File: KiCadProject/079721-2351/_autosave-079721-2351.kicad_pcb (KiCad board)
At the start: 2 copper layers, 227 parts, among them IC1 HC244, IC101 uPC177C, IC201 MP493, IC401 D151811-0360, IC402 IS157, IC501 D151821-0020, IC601 MP5273, IC602 TC4071BP_2, IC603 TC4069UPB_2, J1 Conn_02x13_Odd_Even-MazdaProj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, J2 Conn_02x11_Top_Bottom_Shielde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, J201 Connected, J601 Connected, J711 Empty, Q802 C945, T001 2SB1015B, T211 RN1006, T711 2CS2001, T712 2SD1415, T721 2CS2001, T722 2SD1415, T751 CE1A3Q, T761 CE1A3Q, T801 2CS2001, T803 2CS4065, T811 2CS2001, T812 CE1A3Q, T821 Empty, T822 CE1A3Q (empty), T831 Empty, T832 CE1A3Q (empty), T841 2CS2001, T842 CE1A3Q, T851 Empty, T852 CE1A3Q (empty), T861 Empty, T911 RN1006, T921 RN1006, X601 Crystal

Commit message: Bottom And Top
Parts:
- added J10: Conn_01x01_Female, pinhead-1:pinhead-1-1X01, F.Cu at (196.3, -120.5)
- added J11: Conn_01x01_Female, pinhead-1:pinhead-1-1X01, F.Cu at (200.0, -124.2)
- added J12: Conn_01x01_Female, pinhead-1:pinhead-1-1X01, F.Cu at (203.7, -127.9)
- added J13: Conn_01x01_Female, pinhead-1:pinhead-1-1X01, F.Cu at (192.6, -113.1)
- added J14: Conn_01x01_Female, pinhead-1:pinhead-1-1X01, F.Cu at (196.3, -116.8)
- added J15: Conn_01x01_Female, pinhead-1:pinhead-1-1X01, F.Cu at (200.0, -120.5)
- added J16: Conn_01x01_Female, pinhead-1:pinhead-1-1X01, F.Cu at (203.7, -124.2)
- added J17: Conn_01x01_Female, pinhead-1:pinhead-1-1X01, F.Cu at (207.4, -127.9)
- added J18: Conn_01x01_Female, pinhead-1:pinhead-1-1X01, F.Cu at (196.3, -113.1)
- added J19: Conn_01x01_Female, pinhead-1:pinhead-1-1X01, F.Cu at (200.0, -116.8)
- added J20: Conn_01x01_Female, pinhead-1:pinhead-1-1X01, F.Cu at (203.7, -120.5)
- added J21: Conn_01x01_Female, pinhead-1:pinhead-1-1X01, F.Cu at (207.4, -124.2)
- added J22: Conn_01x01_Female, pinhead-1:pinhead-1-1X01, F.Cu at (211.1, -127.9)
- added J23: Conn_01x01_Female, pinhead-1:pinhead-1-1X01, F.Cu at (200.0, -113.1)
- added J24: Conn_01x01_Female, pinhead-1:pinhead-1-1X01, F.Cu at (203.7, -116.8)
- added J25: Conn_01x01_Female, pinhead-1:pinhead-1-1X01, F.Cu at (207.4, -120.5)
- added J26: Conn_01x01_Female, pinhead-1:pinhead-1-1X01, F.Cu at (211.1, -124.2)
- added J27: Conn_01x01_Female, pinhead-1:pinhead-1-1X01, F.Cu at (214.7, -127.9)
- added J28: Conn_01x01_Female, pinhead-1:pinhead-1-1X01, F.Cu at (203.7, -113.1)
- added J29: Conn_01x01_Female, pinhead-1:pinhead-1-1X01, F.Cu at (207.4, -116.8)
- added J3: Conn_01x01_Female, pinhead-1:pinhead-1-1X01, F.Cu at (184.5, -132.5)
- added J30: Conn_01x01_Female, pinhead-1:pinhead-1-1X01, F.Cu at (211.1, -120.5)
- added J31: Conn_01x01_Female, pinhead-1:pinhead-1-1X01, F.Cu at (214.7, -124.2)
- added J32: Conn_01x01_Female, pinhead-1:pinhead-1-1X01, F.Cu at (218.4, -127.9)
- added J33: Conn_01x01_Female, pinhead-1:pinhead-1-1X01, F.Cu at (207.4, -113.1)
- added J34: Conn_01x01_Female, pinhead-1:pinhead-1-1X01, F.Cu at (211.1, -116.8)
- added J35: Conn_01x01_Female, pinhead-1:pinhead-1-1X01, F.Cu at (214.7, -120.5)
- added J36: Conn_01x01_Female, pinhead-1:pinhead-1-1X01, F.Cu at (218.4, -124.2)
- added J37: Conn_01x01_Female, pinhead-1:pinhead-1-1X01, F.Cu at (222.1, -127.9)
- added J38: Conn_01x01_Female, pinhead-1:pinhead-1-1X01, F.Cu at (211.1, -113.1)
- added J4: Conn_01x01_Female, pinhead-1:pinhead-1-1X01, F.Cu at (188.8, -132.7)
- added J5: Conn_01x01_Female, pinhead-1:pinhead-1-1X01, F.Cu at (196.3, -127.9)
- added J6: Conn_01x01_Female, pinhead-1:pinhead-1-1X01, F.Cu at (192.6, -120.5)
- added J7: Conn_01x01_Female, pinhead-1:pinhead-1-1X01, F.Cu at (196.3, -124.2)
- added J8: Conn_01x01_Female, pinhead-1:pinhead-1-1X01, F.Cu at (200.0, -127.9)
- added J9: Conn_01x01_Female, pinhead-1:pinhead-1-1X01, F.Cu at (192.6, -116.8)
- moved IC201 42.1 mm to (406.7, 26.8)
- renumbered T001 to T1
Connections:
- C2 pad 1: Net-(C2-Pad1) -> Net-(C1-Pad1)
- C4 pad 1: Net-(C4-Pad1) -> Net-(C3-Pad1)
- C422 pad 2: Net-(C422-Pad2) -> Net-(C411-Pad2)
- C451 pad 2: Net-(C451-Pad2) -> Net-(C431-Pad1)
- C452 pad 2: Net-(C452-Pad2) -> Net-(C442-Pad1)
- C471 pad 2: Net-(C471-Pad2) -> Net-(C441-Pad1)
- C472 pad 1: Net-(C472-Pad1) -> Net-(C461-Pad1)
- C502 pad 1: Net-(C502-Pad1) -> Net-(C501-Pad1)
- C502 pad 2: Net-(C502-Pad2) -> Net-(C501-Pad2)
- C503 pad 1: Net-(C503-Pad1) -> Net-(C105-Pad1)
- C504 pad 1: Net-(C504-Pad1) -> Net-(C105-Pad1)
- C511 pad 2: Net-(C511-Pad2) -> Net-(C501-Pad1)
- C52 pad 1: Net-(C52-Pad1) -> GND
- C53 pad 2: Net-(C53-Pad2) -> GND
- C54 pad 2: Net-(C54-Pad2) -> GND
- C55 pad 2: Net-(C55-Pad2) -> GND
- C6 pad 1: Net-(C6-Pad1) -> Net-(C5-Pad1)
- C6 pad 2: Net-(C6-Pad2) -> Net-(C5-Pad2)
- C604 pad 2: Net-(C604-Pad2) -> Net-(C501-Pad1)
- C606 pad 1: Net-(C606-Pad1) -> Net-(C501-Pad1)
- C607 pad 1: Net-(C607-Pad1) -> Net-(C605-Pad1)
- C607 pad 2: Net-(C607-Pad2) -> Net-(C605-Pad2)
- C8 pad 1: Net-(C8-Pad1) -> Net-(C603-Pad2)
- D1 pad 2: Net-(D1-Pad2) -> Net-(C55-Pad1)
- D3 pad 2: Net-(D3-Pad2) -> Net-(C1-Pad1)
- D4 pad 1: Net-(D4-Pad1) -> Net-(C1-Pad1)
- IC1 pad 1: Net-(IC1-Pad1) -> Net-(C1-Pad1)
- IC1 pad 11: Net-(IC1-Pad11) -> Net-(C9-Pad2)
- IC1 pad 4: Net-(IC1-Pad4) -> Net-(C5-Pad1)
- IC101 pad 10: Net-(IC101-Pad10) -> Net-(C101-Pad2)
- IC101 pad 3: Net-(IC101-Pad3) -> Net-(C105-Pad2)
- IC101 pad 5: Net-(IC101-Pad5) -> Net-(C504-Pad2)
- IC101 pad 8: Net-(IC101-Pad8) -> Net-(C111-Pad1)
- IC401 pad 10: Net-(IC401-Pad10) -> Net-(C442-Pad2)
- IC401 pad 11: Net-(IC401-Pad11) -> Net-(C432-Pad1)
- IC401 pad 12: Net-(IC401-Pad12) -> Net-(C422-Pad1)
- IC401 pad 15: Net-(IC401-Pad15) -> Net-(C405-Pad1)
- IC401 pad 16: Net-(IC401-Pad16) -> Net-(C405-Pad1)
- IC401 pad 18: Net-(IC401-Pad18) -> Net-(C405-Pad2)
- IC401 pad 19: Net-(IC401-Pad19) -> Net-(C491-Pad2)
- IC401 pad 7: Net-(IC401-Pad7) -> Net-(C472-Pad2)
- IC401 pad 8: Net-(IC401-Pad8) -> Net-(C461-Pad2)
- IC401 pad 9: Net-(IC401-Pad9) -> Net-(C452-Pad1)
- IC402 pad 6: Net-(IC402-Pad6) -> Net-(C405-Pad1)
- IC501 pad 13: Net-(IC501-Pad13) -> Net-(C502-Pad7)
- IC501 pad 14: Net-(IC501-Pad14) -> Net-(C501-Pad7)
- IC501 pad 15: Net-(IC501-Pad15) -> Net-(C501-Pad6)
- IC501 pad 16: Net-(IC501-Pad16) -> Net-(C502-Pad5)
- IC501 pad 17: Net-(IC501-Pad17) -> Net-(C501-Pad5)
- IC501 pad 18: Net-(IC501-Pad18) -> Net-(C501-Pad4)
- IC501 pad 19: Net-(IC501-Pad19) -> Net-(C501-Pad3)
- IC501 pad 20: Net-(IC501-Pad20) -> Net-(C501-Pad2)
- IC601 pad 11: Net-(IC601-Pad11) -> Net-(IC101-Pad1)
- IC601 pad 12: Net-(IC601-Pad12) -> Net-(IC501-Pad6)
- IC601 pad 14: Net-(IC601-Pad14) -> Net-(IC501-Pad4)
- IC601 pad 15: Net-(IC601-Pad15) -> Net-(IC501-Pad5)
- IC601 pad 16: Net-(IC601-Pad16) -> Net-(IC501-Pad10)
- IC601 pad 28: Net-(IC601-Pad28) -> Net-(IC1-Pad12)
- IC601 pad 32: Net-(IC601-Pad32) -> Net-(IC401-Pad23)
- IC601 pad 33: Net-(IC601-Pad33) -> Net-(IC401-Pad22)
- IC601 pad 34: Net-(IC601-Pad34) -> Net-(IC401-Pad21)
- IC601 pad 39: Net-(IC601-Pad39) -> Net-(C9-Pad1)
- IC602 pad 14: Net-(IC602-Pad14) -> Net-(C605-Pad1)
- IC602 pad 3: Net-(IC602-Pad3) -> Net-(IC201-Pad7)
- IC602 pad 4: Net-(IC602-Pad4) -> Net-(IC201-Pad4)
- IC602 pad 5: Net-(IC602-Pad5) -> Net-(IC602-Pad2)
- IC602 pad 9: Net-(IC602-Pad9) -> Net-(IC602-Pad2)
- IC603 pad 1: Net-(IC603-Pad1) -> Net-(IC101-Pad13)
- IC603 pad 14: Net-(IC603-Pad14) -> Net-(C605-Pad1)
- IC603 pad 5: Net-(IC603-Pad5) -> Net-(IC401-Pad17)
- IC603 pad 6: Net-(IC603-Pad6) -> Net-(IC602-Pad12)
- IC603 pad 9: Net-(IC603-Pad9) -> Net-(IC101-Pad14)
- J1 pad 2B: Net-(J1-Pad2B) -> Net-(J1-Pad2A)
- J1 pad 2K: Net-(J1-Pad2K) -> Net-(F401-Pad1)
- J1 pad 2M: Net-(J1-Pad2M) -> Net-(C441-Pad2)
- J1 pad 2O: Net-(J1-Pad2O) -> Net-(C451-Pad1)
- J1 pad 2P: Net-(J1-Pad2P) -> Net-(C421-Pad2)
- J1 pad 2Q: Net-(J1-Pad2Q) -> Net-(C431-Pad2)
- J2 pad B: Net-(J2-PadB) -> Net-(C56-Pad1)
- J2 pad D: Net-(J2-PadD) -> Net-(C911-Pad1)
- J2 pad F: Net-(J2-PadF) -> Net-(C921-Pad1)
- J2 pad M: Net-(J2-PadM) -> Net-(J2-PadL)
- J2 pad T: Net-(J2-PadT) -> Net-(J1-Pad2I)
- J201 pad 1: Net-(J201-Pad1) -> Net-(IC201-Pad2)
- J601 pad 1: Net-(J601-Pad1) -> Net-(IC1-Pad7)
- J601 pad 2: Net-(J601-Pad2) -> Net-(IC601-Pad29)
- J711 pad 1: Net-(J711-Pad1) -> Net-(C721-Pad2)
- J711 pad 2: Net-(J711-Pad2) -> Net-(C711-Pad2)
- R1 pad 1: Net-(R1-Pad1) -> Net-(IC1-Pad2)
- R101 pad 1: Net-(R101-Pad1) -> Net-(J1-Pad2E)
- R102 pad 1: Net-(R102-Pad1) -> Net-(C101-Pad2)
- R102 pad 2: Net-(R102-Pad2) -> Net-(J1-Pad2E)
- R104 pad 1: Net-(R104-Pad1) -> Net-(C101-Pad1)
- R104 pad 2: Net-(R104-Pad2) -> Net-(IC101-Pad11)
- R105 pad 1: Net-(R105-Pad1) -> Net-(IC101-Pad13)
- R105 pad 2: Net-(R105-Pad2) -> Net-(IC101-Pad11)
- R106 pad 1: Net-(R106-Pad1) -> Net-(C405-Pad1)
- R111 pad 1: Net-(R111-Pad1) -> Net-(J1-Pad2G)
- R112 pad 1: Net-(R112-Pad1) -> Net-(C111-Pad1)
- R112 pad 2: Net-(R112-Pad2) -> Net-(J1-Pad2G)
- R114 pad 2: Net-(R114-Pad2) -> Net-(C101-Pad1)
- R115 pad 2: Net-(R115-Pad2) -> Net-(IC101-Pad14)
- R116 pad 1: Net-(R116-Pad1) -> Net-(C405-Pad1)
- R2 pad 2: Net-(R2-Pad2) -> Net-(C9-Pad1)
- R204 pad 1: Net-(R204-Pad1) -> Net-(IC201-Pad24)
- R21 pad 1: Net-(R21-Pad1) -> Net-(C1-Pad1)
- R401 pad 1: Net-(R401-Pad1) -> Net-(J1-Pad2N)
- R402 pad 1: Net-(R402-Pad1) -> Net-(C401-Pad2)
- R414 pad 1: Net-(R414-Pad1) -> Net-(IC401-Pad13)
- R422 pad 1: Net-(R422-Pad1) -> Net-(C422-Pad1)
- R422 pad 2: Net-(R422-Pad2) -> Net-(C421-Pad2)
- R431 pad 1: Net-(R431-Pad1) -> Net-(C431-Pad2)
- R432 pad 1: Net-(R432-Pad1) -> Net-(C432-Pad1)
- R441 pad 2: Net-(R441-Pad2) -> Net-(C441-Pad2)
- R442 pad 1: Net-(R442-Pad1) -> Net-(C442-Pad2)
- R442 pad 2: Net-(R442-Pad2) -> Net-(C441-Pad2)
- R451 pad 1: Net-(R451-Pad1) -> Net-(C451-Pad1)
- R452 pad 1: Net-(R452-Pad1) -> Net-(C452-Pad1)
- R452 pad 2: Net-(R452-Pad2) -> Net-(C451-Pad1)
- R461 pad 1: Net-(R461-Pad1) -> Net-(C405-Pad1)
- R461 pad 2: Net-(R461-Pad2) -> Net-(IC402-Pad7)
- R471 pad 1: Net-(R471-Pad1) -> Net-(J1-Pad2L)
- R472 pad 1: Net-(R472-Pad1) -> Net-(C472-Pad2)
- R481 pad 1: Net-(R481-Pad1) -> Net-(R111-Pad2)
- R481 pad 2: Net-(R481-Pad2) -> Net-(J1-Pad2J)
- R482 pad 2: Net-(R482-Pad2) -> Net-(J1-Pad2J)
- R483 pad 1: Net-(R483-Pad1) -> Net-(R412-Pad2)
- R483 pad 2: Net-(R483-Pad2) -> Net-(C481-Pad2)
- R491 pad 2: Net-(R491-Pad2) -> Net-(J1-Pad2H)
- R492 pad 1: Net-(R492-Pad1) -> Net-(C491-Pad2)
- R492 pad 2: Net-(R492-Pad2) -> Net-(J1-Pad2H)
- R493 pad 1: Net-(R493-Pad1) -> Net-(C491-Pad2)
- R501 pad 2: Net-(R501-Pad2) -> Net-(J2-PadP)
- R502 pad 2: Net-(R502-Pad2) -> Net-(J2-PadU)
- R506 pad 1: Net-(R506-Pad1) -> Net-(J2-PadS)
- R507 pad 2: Net-(R507-Pad2) -> Net-(J2-PadO)
- R509 pad 2: Net-(R509-Pad2) -> Net-(J1-Pad2I)
- R510 pad 1: Net-(R510-Pad1) -> Net-(J1-Pad2I)
- R511 pad 2: Net-(R511-Pad2) -> Net-(J2-PadU)
- R512 pad 2: Net-(R512-Pad2) -> Net-(J2-PadO)
- R513 pad 1: Net-(R513-Pad1) -> Net-(C501-Pad6)
- R514 pad 1: Net-(R514-Pad1) -> Net-(C502-Pad5)
- R514 pad 2: Net-(R514-Pad2) -> Net-(J2-PadN)
- R515 pad 2: Net-(R515-Pad2) -> Net-(R505-Pad2)
- R516 pad 1: Net-(R516-Pad1) -> Net-(C501-Pad4)
- R516 pad 2: Net-(R516-Pad2) -> Net-(R504-Pad2)
- R517 pad 2: Net-(R517-Pad2) -> Net-(R503-Pad2)
- R518 pad 2: Net-(R518-Pad2) -> Net-(J2-PadP)
- R519 pad 2: Net-(R519-Pad2) -> Net-(J1-Pad2I)
- R520 pad 2: Net-(R520-Pad2) -> Net-(R508-Pad2)
- R531 pad 2: Net-(R531-Pad2) -> Net-(J2-PadV)
- R532 pad 1: Net-(R532-Pad1) -> Net-(J2-PadR)
- R541 pad 2: Net-(R541-Pad2) -> Net-(J2-PadV)
- R542 pad 2: Net-(R542-Pad2) -> Net-(J2-PadR)
- R561 pad 1: Net-(R561-Pad1) -> Net-(IC101-Pad6)
- R562 pad 1: Net-(R562-Pad1) -> Net-(C105-Pad1)
- R601 pad 3: Net-(R601-Pad3) -> Net-(IC601-Pad8)
- R601 pad 4: Net-(R601-Pad4) -> Net-(IC601-Pad7)
- R601 pad 6: Net-(R601-Pad6) -> Net-(IC601-Pad37)
- R601 pad 7: Net-(R601-Pad7) -> Net-(IC601-Pad38)
- R601 pad 8: Net-(R601-Pad8) -> Net-(IC601-Pad40)
- R601 pad 9: Net-(R601-Pad9) -> Net-(IC601-Pad42)
- R602 pad 1: Net-(R602-Pad1) -> Net-(IC601-Pad19)
- R602 pad 2: Net-(R602-Pad2) -> Net-(IC101-Pad1)
- R602 pad 3: Net-(R602-Pad3) -> Net-(IC601-Pad10)
- R602 pad 4: Net-(R602-Pad4) -> Net-(IC101-Pad13)
- R602 pad 5: Net-(R602-Pad5) -> Net-(C405-Pad1)
- R602 pad 6: Net-(R602-Pad6) -> Net-(IC101-Pad14)
- R602 pad 7: Net-(R602-Pad7) -> Net-(IC601-Pad6)
- R602 pad 8: Net-(R602-Pad8) -> Net-(IC601-Pad5)
- R602 pad 9: Net-(R602-Pad9) -> Net-(IC603-Pad11)
- R712 pad 2: Net-(R712-Pad2) -> Net-(R711-Pad2)
- R722 pad 1: Net-(R722-Pad1) -> Net-(R721-Pad2)
- R763 pad 1: Net-(R763-Pad1) -> Net-(R753-Pad1)
- R802 pad 2: Net-(R802-Pad2) -> Net-(D801-Pad1)
- R803 pad 1: Net-(R803-Pad1) -> Net-(R801-Pad2)
- R803 pad 2: Net-(R803-Pad2) -> Net-(Q802-Pad1)
- R804 pad 2: Net-(R804-Pad2) -> Net-(Q802-Pad1)
- R807 pad 1: Net-(R807-Pad1) -> Net-(D802-Pad2)
- R812 pad 1: Net-(R812-Pad1) -> Net-(D812-Pad2)
- R812 pad 2: Net-(R812-Pad2) -> Net-(J1-Pad2X)
- R813 pad 2: Net-(R813-Pad2) -> Net-(D811-Pad2)
- R822 pad 1: Net-(R822-Pad1) -> Net-(D821-Pad2)
- R822 pad 2: Net-(R822-Pad2) -> Net-(J1-Pad2S)
- R832 pad 1: Net-(R832-Pad1) -> Net-(D831-Pad2)
- R832 pad 2: Net-(R832-Pad2) -> Net-(J1-Pad2T)
- R842 pad 2: Net-(R842-Pad2) -> Net-(J2-PadJ)
- R861 pad 2: Net-(R861-Pad2) -> Net-(J1-Pad2Y)
- R912 pad 1: Net-(R912-Pad1) -> Net-(C1-Pad1)
- R913 pad 2: Net-(R913-Pad2) -> Net-(C911-Pad1)
- R923 pad 2: Net-(R923-Pad2) -> Net-(C921-Pad1)
- R924 pad 2: Net-(R924-Pad2) -> Net-(J2-PadE)
- T1 pad 2: Net-(T001-Pad2) -> Net-(C5-Pad1)
- T1 pad 3: Net-(T001-Pad3) -> Net-(IC1-Pad2)
- T711 pad 1: Net-(T711-Pad1) -> Net-(IC201-Pad24)
- T711 pad 3: Net-(T711-Pad3) -> Net-(IC201-Pad19)
- T712 pad 1: Net-(T712-Pad1) -> Net-(R711-Pad2)
- T721 pad 1: Net-(T721-Pad1) -> Net-(IC201-Pad24)
- T721 pad 3: Net-(T721-Pad3) -> Net-(IC201-Pad18)
- T722 pad 1: Net-(T722-Pad1) -> Net-(R721-Pad2)
- T751 pad 1: Net-(T751-Pad1) -> Net-(J1-Pad2C)
- T761 pad 1: Net-(T761-Pad1) -> Net-(J1-Pad2C)
- T801 pad 1: Net-(T801-Pad1) -> Net-(IC201-Pad24)
- T801 pad 3: Net-(T801-Pad3) -> Net-(IC201-Pad17)
- T803 pad 2: Net-(T803-Pad2) -> Net-(R807-Pad2)
- T811 pad 1: Net-(T811-Pad1) -> Net-(R761-Pad2)
- T811 pad 3: Net-(T811-Pad3) -> Net-(R814-Pad1)
- T812 pad 3: Net-(T812-Pad3) -> Net-(R811-Pad2)
- T821 pad 1: Net-(T821-Pad1) -> Net-(R761-Pad2)
- T821 pad 3: Net-(T821-Pad3) -> Net-(R823-Pad1)
- T822 pad 3: Net-(T822-Pad3) -> Net-(R821-Pad2)
- T831 pad 1: Net-(T831-Pad1) -> Net-(R761-Pad2)
- T831 pad 3: Net-(T831-Pad3) -> Net-(R833-Pad1)
- T841 pad 1: Net-(T841-Pad1) -> Net-(R761-Pad2)
- T841 pad 3: Net-(T841-Pad3) -> Net-(R843-Pad1)
- T851 pad 1: Net-(T851-Pad1) -> Net-(IC201-Pad24)
- T911 pad 1: Net-(T911-Pad1) -> Net-(C7-Pad2)
- c51 pad 2: Net-(c51-Pad2) -> GND
- c861 pad 1: Net-(c861-Pad1) -> Net-(J1-Pad2Y)

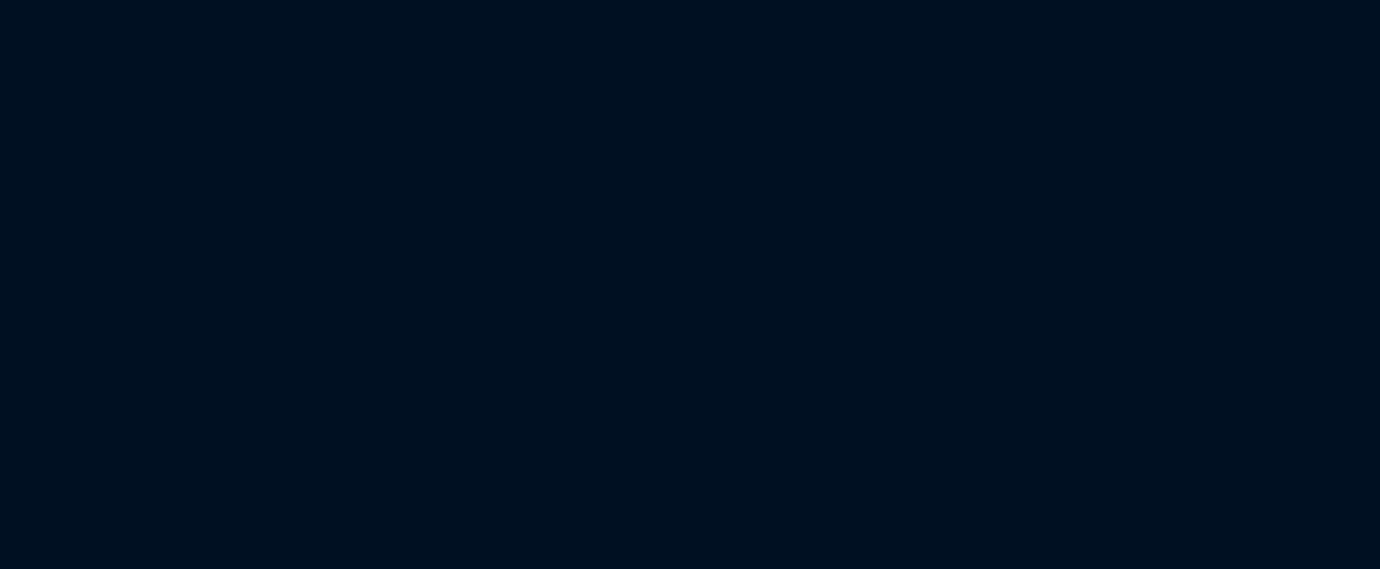
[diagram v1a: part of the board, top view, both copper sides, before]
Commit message: Bottom: wires -> labels
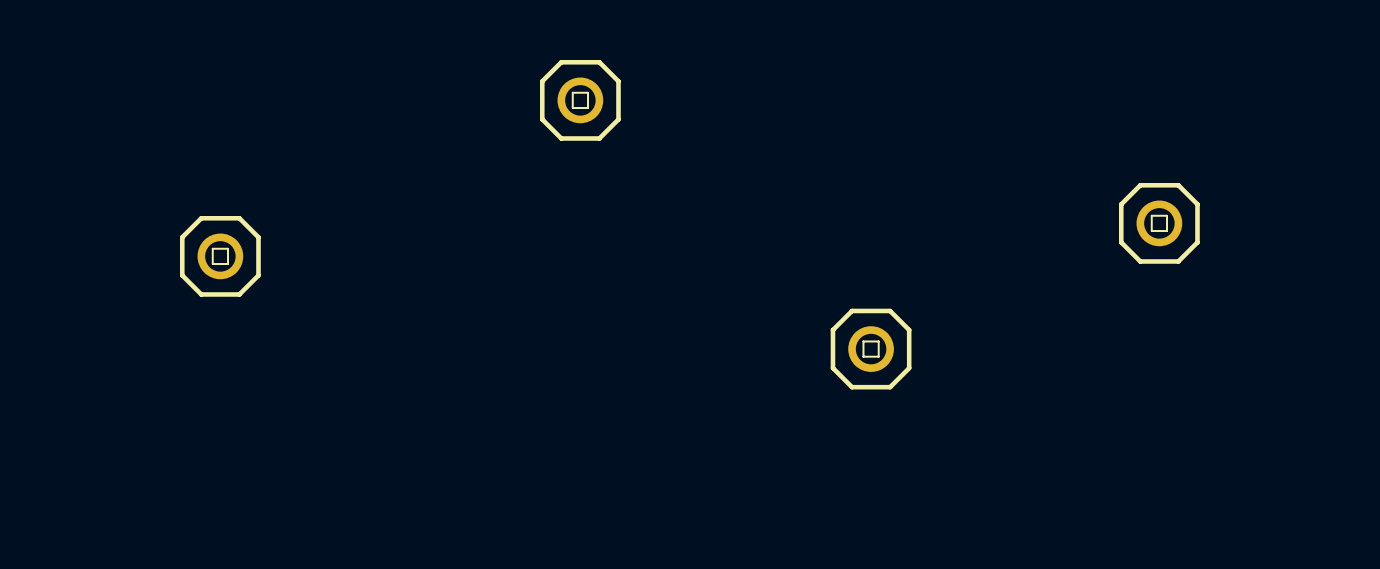
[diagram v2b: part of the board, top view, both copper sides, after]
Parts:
- added J39: Conn_01x01_Female, pinhead-1:pinhead-1-1X01, F.Cu at (231.9, -170.2)
- added J40: Conn_01x01_Female, pinhead-1:pinhead-1-1X01, F.Cu at (243.9, -175.4)
- added J41: Conn_01x01_Female, pinhead-1:pinhead-1-1X01, F.Cu at (263.2, -171.3)
- added J42: Conn_01x01_Female, pinhead-1:pinhead-1-1X01, F.Cu at (253.6, -167.1)
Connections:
- T911 pad 1: Net-(C7-Pad2) -> Net-(T911-Pad1)
- T911 pad 3: Net-(J23-Pad1) -> Net-(T911-Pad3)
